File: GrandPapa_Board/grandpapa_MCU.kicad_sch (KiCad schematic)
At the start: 1 part, among them U1 DSPIC33EP512GP502

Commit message: Shameless papa copying pt 1
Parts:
- removed U1: DSPIC33EP512GP502, Package_DIP:DIP-28_W7.62mm, symbol CANHW:DSPIC33EP512GP502
- added U?: PIC18F26K83, symbol CANHW:PIC18F26K83
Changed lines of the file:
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@@
 (kicad_sch (version 20211123) (generator eeschema)
   (paper "A4")
-  (symbol (lib_id "CANHW:DSPIC33EP512GP502") (at 93.98 128.27 0) (unit 1)
+  (symbol (lib_id "CANHW:PIC18F26K83") (at 137.16 99.06 0) (unit 1)
     (in_bom yes) (on_board yes) (fields_autoplaced)
-    (property "Reference" "U1" (id 0) (at 98.5394 95.25 0)
-      (effects (font (size 1.27 1.27)) (justify left))
-    )
-    (property "Value" "DSPIC33EP512GP502" (id 1) (at 98.5394 97.79 0)
-      (effects (font (size 1.27 1.27)) (justify left))
-    )
-    (property "Footprint" "Package_DIP:DIP-28_W7.62mm" (id 2) (at 93.98 128.27 0)
+    (property "Reference" "U?" (id 0) (at 136.525 74.93 0))
+    (property "Value" "PIC18F26K83" (id 1) (at 136.525 77.47 0))
+    (property "Footprint" "" (id 2) (at 148.59 99.06 0)
       (effects (font (size 1.27 1.27)) hide)
     )
-    (property "Datasheet" "" (id 3) (at 93.98 128.27 0)
+    (property "Datasheet" "http://ww1.microchip.com/downloads/en/DeviceDoc/40001943A.pdf" (id 3) (at 148.59 99.06 0)
       (effects (font (size 1.27 1.27)) hide)
     )

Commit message: Add power circuits and some PIC stuff, grandpapa lib
5V buck, 3.3V LDO, load switches, current and voltage sensing, some PIC stuff
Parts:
- added C? (x2): 0.1uF 20V, symbol Device:C_Small
- added C? (x2): 27pF, Capacitor_SMD:C_0805_2012Metric_Pad1.18x1.45mm_HandSolder, symbol Device:C_Small
- added D?: QBLP650-IW, LED_SMD:LED_1206_3216Metric_Pad1.42x1.75mm_HandSolder, symbol Device:LED
- added D?: 150120BS75000, LED_SMD:LED_1206_3216Metric_Pad1.42x1.75mm_HandSolder, symbol Device:LED
- added D?: 156120RS75000, LED_SMD:LED_1206_3216Metric_Pad1.42x1.75mm_HandSolder, symbol Device:LED
- added J?: Programming Header, canhw_footprints:PinHeader_5x2.54_SMD_90deg_952-3198-1-ND, symbol sensors-rescue:Conn_01x05_Female-Connector
- added R? (x3): 150R, Resistor_SMD:R_0805_2012Metric_Pad1.20x1.40mm_HandSolder, symbol Device:R_Small_US
- added R?: 100R, symbol Device:R_Small_US
- added R?: 10kR, symbol Device:R_Small_US
- added Y?: 12MHz, Crystal:Crystal_HC49-4H_Vertical, symbol Device:Crystal
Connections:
- net at U?.1 (~{MCLR}): now also R?.2
- net at U?.10 (RA6/OSC2): now also C?.1, Y?.2
- net MOSI: now reaches U?.13 (RC2)
- net MOSI: now also U?.15 (RC4)
- net SCK: now reaches U?.14 (RC3)
- net at U?.16 (RC5): now also R?.1
- net at U?.17 (RC6): now also R?.1
- net at U?.18 (RC7): now also R?.1
- net GND: now reaches U?.19 (VSS)
- net GND: now also U?.8 (VSS), C?.2, C?.2, C?.2, C?.2, D?.1 (K), D?.1 (K), D?.1 (K), J?.3 (Pin_3)
- net BATT_CURR_AMP: now reaches U?.2 (RA0)
- net +3V3: now reaches U?.20 (VDD)
- net +3V3: now also C?.1, J?.2 (Pin_2), R?.1
- net MINISENSOR_PWR_EN: now reaches U?.24 (RB3)
- net STRAIN_GUAGE_AMP_PWR_EN: now reaches U?.25 (RB4)
- net LOGGER_PWR_EN: now reaches U?.26 (RB5)
- net ICSPCLK: now reaches U?.27 (RB6/ICSPCLK)
- net ICSPCLK: now also J?.5 (Pin_5)
- net ICSPDAT: now reaches U?.28 (RB7/ICSPDAT)
- net ICSPDAT: now also J?.4 (Pin_4)
- net 3V3_CURR_AMP: now reaches U?.3 (RA1)
- net V_SENSE: now reaches U?.4 (RA2)
- net CS: now reaches U?.7 (RA5)
- net at U?.9 (RA7/OSC1): now also C?.1, Y?.1
- new net: D?.2 (A), R?.2 (x3)
- new net ~{MCLR}: C?.1, J?.1 (Pin_1), R?.1, R?.2
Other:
- note added: "BLUE"
- note added: "Debugging LEDs Vs = 3.3V"
- note added: "ENABLE AT >1.3V"
- note added: "RED"
- note added: "WHITE"

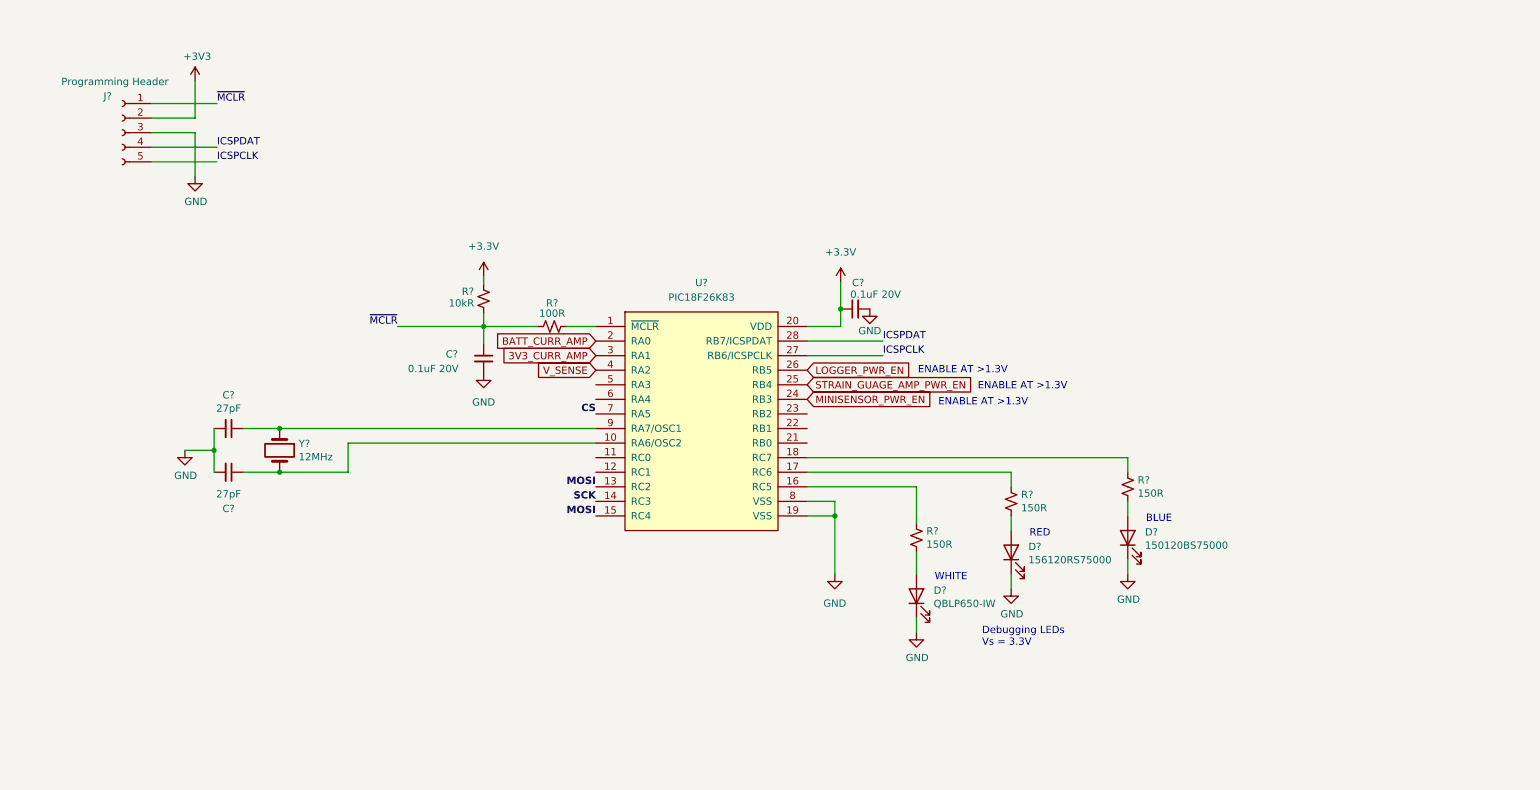
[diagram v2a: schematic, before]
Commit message: Add missing capacitor value, annotate symbols
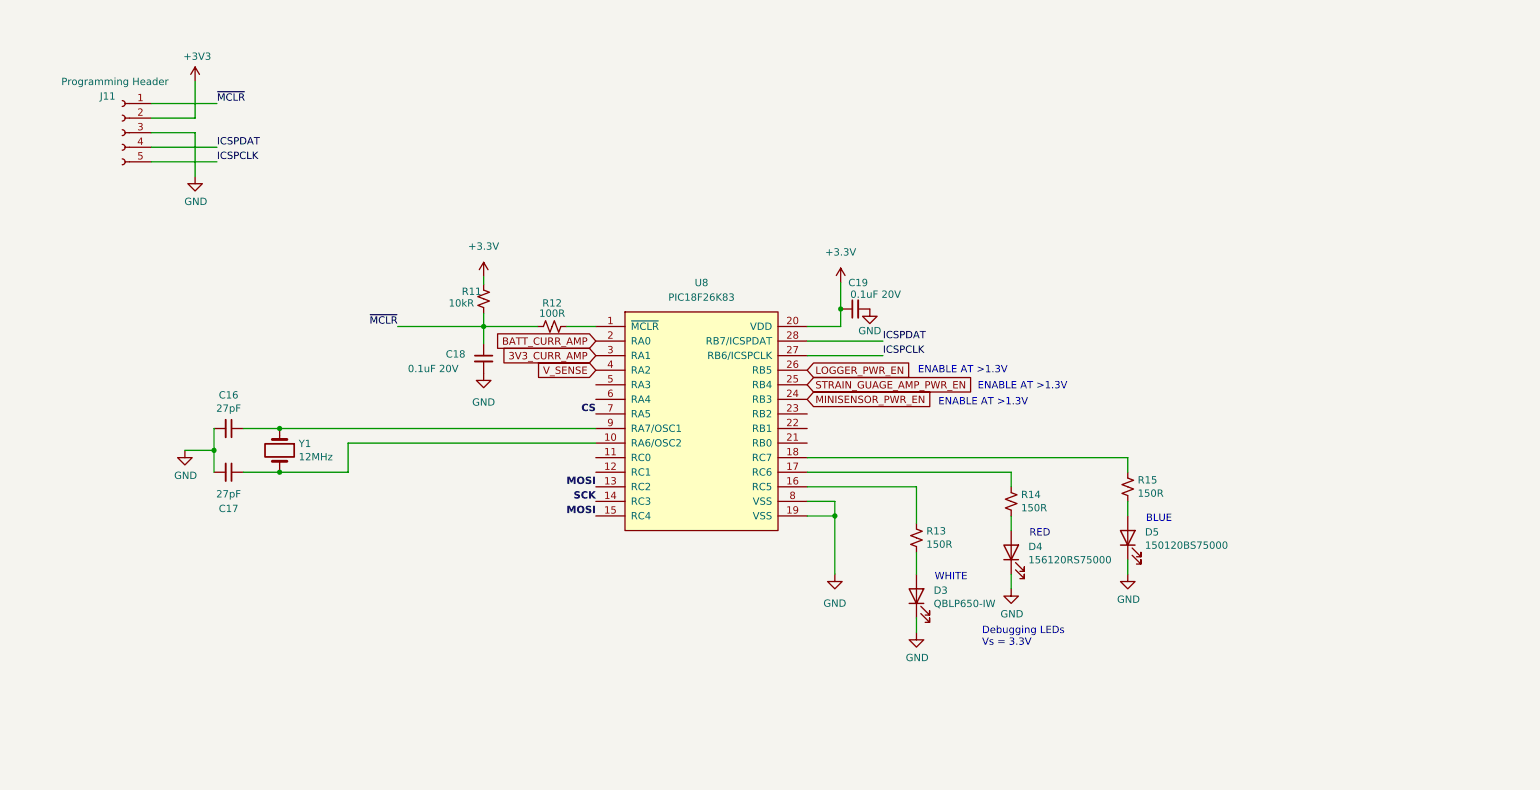
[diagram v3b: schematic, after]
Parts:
- gave numbers to parts that had none: 15
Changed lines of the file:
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@@
   (symbol (lib_id "Device:R_Small_US") (at 190.5 113.03 0) (unit 1)
     (in_bom yes) (on_board yes)
-    (property "Reference" "R?" (id 0) (at 192.2272 111.8616 0)
+    (property "Reference" "R14" (id 0) (at 192.2272 111.8616 0)
       (effects (font (size 1.27 1.27)) (justify left))
     )
@@
   (symbol (lib_id "power:+3V3") (at 48.26 39.878 0) (unit 1)
     (in_bom yes) (on_board yes)
-    (property "Reference" "#PWR?" (id 0) (at 48.26 43.688 0)
+    (property "Reference" "#PWR040" (id 0) (at 48.26 43.688 0)
       (effects (font (size 1.27 1.27)) hide)
     )
@@
   (symbol (lib_id "sensors-rescue:Conn_01x05_Female-Connector") (at 35.56 48.768 0) (mirror y) (unit 1)
     (in_bom yes) (on_board yes)
-    (property "Reference" "J?" (id 0) (at 33.02 42.418 0))
+    (property "Reference" "J11" (id 0) (at 33.02 42.418 0))
     (property "Value" "Programming Header" (id 1) (at 34.29 39.878 0))
     (property "Footprint" "canhw_footprints:PinHeader_5x2.54_SMD_90deg_952-3198-1-ND" (id 2) (at 35.56 48.768 0)
@@
   (symbol (lib_id "power:GND") (at 210.82 125.73 0) (unit 1)
     (in_bom yes) (on_board yes)
-    (property "Reference" "#PWR?" (id 0) (at 210.82 132.08 0)
+    (property "Reference" "#PWR049" (id 0) (at 210.82 132.08 0)
       (effects (font (size 1.27 1.27)) hide)
     )
@@
   (symbol (lib_id "power:GND") (at 46.482 104.14 0) (unit 1)
     (in_bom yes) (on_board yes)
-    (property "Reference" "#PWR?" (id 0) (at 46.482 110.49 0)
+    (property "Reference" "#PWR039" (id 0) (at 46.482 110.49 0)
       (effects (font (size 1.27 1.27)) hide)
     )
@@
   (symbol (lib_id "power:GND") (at 165.862 79.502 0) (unit 1)
     (in_bom yes) (on_board yes)
-    (property "Reference" "#PWR?" (id 0) (at 165.862 85.852 0)
+    (property "Reference" "#PWR046" (id 0) (at 165.862 85.852 0)
       (effects (font (size 1.27 1.27)) hide)
     )
@@
   (symbol (lib_id "Device:LED") (at 173.99 129.54 90) (unit 1)
     (in_bom yes) (on_board yes)
-    (property "Reference" "D?" (id 0) (at 176.9872 128.5494 90)
+    (property "Reference" "D3" (id 0) (at 176.9872 128.5494 90)
       (effects (font (size 1.27 1.27)) (justify right))
     )
@@
   (symbol (lib_id "power:GND") (at 159.766 125.73 0) (unit 1)
     (in_bom yes) (on_board yes) (fields_autoplaced)
-    (property "Reference" "#PWR?" (id 0) (at 159.766 132.08 0)
+    (property "Reference" "#PWR044" (id 0) (at 159.766 132.08 0)
       (effects (font (size 1.27 1.27)) hide)
     )
@@
   (symbol (lib_id "Device:C_Small") (at 98.552 88.138 0) (unit 1)
     (in_bom yes) (on_board yes)
-    (property "Reference" "C?" (id 0) (at 91.948 87.376 0)
+    (property "Reference" "C18" (id 0) (at 91.948 87.376 0)
       (effects (font (size 1.27 1.27)) (justify left))
     )
@@
   (symbol (lib_id "Device:R_Small_US") (at 173.99 119.38 0) (unit 1)
     (in_bom yes) (on_board yes)
-    (property "Reference" "R?" (id 0) (at 175.7172 118.2116 0)
+    (property "Reference" "R13" (id 0) (at 175.7172 118.2116 0)
       (effects (font (size 1.27 1.27)) (justify left))
     )
@@
   (symbol (lib_id "Device:R_Small_US") (at 210.82 110.49 0) (unit 1)
     (in_bom yes) (on_board yes)
-    (property "Reference" "R?" (id 0) (at 212.5472 109.3216 0)
+    (property "Reference" "R15" (id 0) (at 212.5472 109.3216 0)
       (effects (font (size 1.27 1.27)) (justify left))
     )
@@
   (symbol (lib_id "power:+3.3V") (at 98.552 73.914 0) (unit 1)
     (in_bom yes) (on_board yes) (fields_autoplaced)
-    (property "Reference" "#PWR?" (id 0) (at 98.552 77.724 0)
+    (property "Reference" "#PWR042" (id 0) (at 98.552 77.724 0)
       (effects (font (size 1.27 1.27)) hide)
     )
@@
   (symbol (lib_id "Device:R_Small_US") (at 110.49 82.55 90) (unit 1)
     (in_bom yes) (on_board yes)
-    (property "Reference" "R?" (id 0) (at 110.49 78.486 90))
+    (property "Reference" "R12" (id 0) (at 110.49 78.486 90))
     (property "Value" "100R" (id 1) (at 110.49 80.264 90))
     (property "Footprint" "" (id 2) (at 110.49 82.55 0)
@@
   (symbol (lib_id "power:GND") (at 98.552 90.678 0) (unit 1)
     (in_bom yes) (on_board yes) (fields_autoplaced)
-    (property "Reference" "#PWR?" (id 0) (at 98.552 97.028 0)
+    (property "Reference" "#PWR043" (id 0) (at 98.552 97.028 0)
       (effects (font (size 1.27 1.27)) hide)
     )
@@
   (symbol (lib_id "Device:C_Small") (at 163.322 79.502 90) (unit 1)
     (in_bom yes) (on_board yes)
-    (property "Reference" "C?" (id 0) (at 163.83 74.93 90))
+    (property "Reference" "C19" (id 0) (at 163.83 74.93 90))
     (property "Value" "0.1uF 20V" (id 1) (at 166.878 76.962 90))
     (property "Footprint" "" (id 2) (at 163.322 79.502 0)
@@
   (symbol (lib_id "Device:LED") (at 210.82 119.38 90) (unit 1)
     (in_bom yes) (on_board yes)
-    (property "Reference" "D?" (id 0) (at 213.8172 118.3894 90)
+    (property "Reference" "D5" (id 0) (at 213.8172 118.3894 90)
       (effects (font (size 1.27 1.27)) (justify right))
     )
@@
   (symbol (lib_id "Device:C_Small") (at 54.102 107.95 270) (unit 1)
     (in_bom yes) (on_board yes)
-    (property "Reference" "C?" (id 0) (at 54.102 114.3 90))
+    (property "Reference" "C17" (id 0) (at 54.102 114.3 90))
     (property "Value" "27pF" (id 1) (at 54.102 111.76 90))
     (property "Footprint" "Capacitor_SMD:C_0805_2012Metric_Pad1.18x1.45mm_HandSolder" (id 2) (at 54.102 107.95 0)
@@
   (symbol (lib_id "power:GND") (at 48.26 56.388 0) (unit 1)
     (in_bom yes) (on_board yes)
-    (property "Reference" "#PWR?" (id 0) (at 48.26 62.738 0)
+    (property "Reference" "#PWR041" (id 0) (at 48.26 62.738 0)
       (effects (font (size 1.27 1.27)) hide)
     )
@@
   (symbol (lib_id "power:+3.3V") (at 160.782 74.93 0) (unit 1)
     (in_bom yes) (on_board yes) (fields_autoplaced)
-    (property "Reference" "#PWR?" (id 0) (at 160.782 78.74 0)
+    (property "Reference" "#PWR045" (id 0) (at 160.782 78.74 0)
       (effects (font (size 1.27 1.27)) hide)
     )
@@
   (symbol (lib_id "Device:LED") (at 190.5 121.92 90) (unit 1)
     (in_bom yes) (on_board yes)
-    (property "Reference" "D?" (id 0) (at 193.4972 120.9294 90)
+    (property "Reference" "D4" (id 0) (at 193.4972 120.9294 90)
       (effects (font (size 1.27 1.27)) (justify right))
     )
@@
   (symbol (lib_id "CANHW:PIC18F26K83") (at 137.16 99.06 0) (unit 1)
     (in_bom yes) (on_board yes) (fields_autoplaced)
-    (property "Reference" "U?" (id 0) (at 136.525 74.93 0))
+    (property "Reference" "U8" (id 0) (at 136.525 74.93 0))
     (property "Value" "PIC18F26K83" (id 1) (at 136.525 77.47 0))
     (property "Footprint" "" (id 2) (at 148.59 99.06 0)
@@
   (symbol (lib_id "power:GND") (at 190.5 128.27 0) (unit 1)
     (in_bom yes) (on_board yes)
-    (property "Reference" "#PWR?" (id 0) (at 190.5 134.62 0)
+    (property "Reference" "#PWR048" (id 0) (at 190.5 134.62 0)
       (effects (font (size 1.27 1.27)) hide)
     )
@@
   (symbol (lib_id "Device:C_Small") (at 54.102 100.33 270) (unit 1)
     (in_bom yes) (on_board yes)
-    (property "Reference" "C?" (id 0) (at 54.102 94.5134 90))
+    (property "Reference" "C16" (id 0) (at 54.102 94.5134 90))
     (property "Value" "27pF" (id 1) (at 54.102 96.8248 90))
     (property "Footprint" "Capacitor_SMD:C_0805_2012Metric_Pad1.18x1.45mm_HandSolder" (id 2) (at 54.102 100.33 0)
@@
   (symbol (lib_id "Device:R_Small_US") (at 98.552 77.724 0) (unit 1)
     (in_bom yes) (on_board yes)
-    (property "Reference" "R?" (id 0) (at 94.742 76.454 0)
+    (property "Reference" "R11" (id 0) (at 94.742 76.454 0)
       (effects (font (size 1.27 1.27)) (justify left))
     )
@@
   (symbol (lib_id "Device:Crystal") (at 62.992 104.14 270) (unit 1)
     (in_bom yes) (on_board yes)
-    (property "Reference" "Y?" (id 0) (at 66.3194 102.9716 90)
+    (property "Reference" "Y1" (id 0) (at 66.3194 102.9716 90)
       (effects (font (size 1.27 1.27)) (justify left))
     )
@@
   (symbol (lib_id "power:GND") (at 173.99 135.89 0) (unit 1)
     (in_bom yes) (on_board yes)
-    (property "Reference" "#PWR?" (id 0) (at 173.99 142.24 0)
-      (effects (font (size 1.27 1.27)) hide)
-    )
+    (property "Reference" "#PWR047" (id 0) (at 173.99 142.24 0)
+      (effects (font (size 1.27 1.27)) hide)
+    )

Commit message: Add motor current sense amp and board output connections
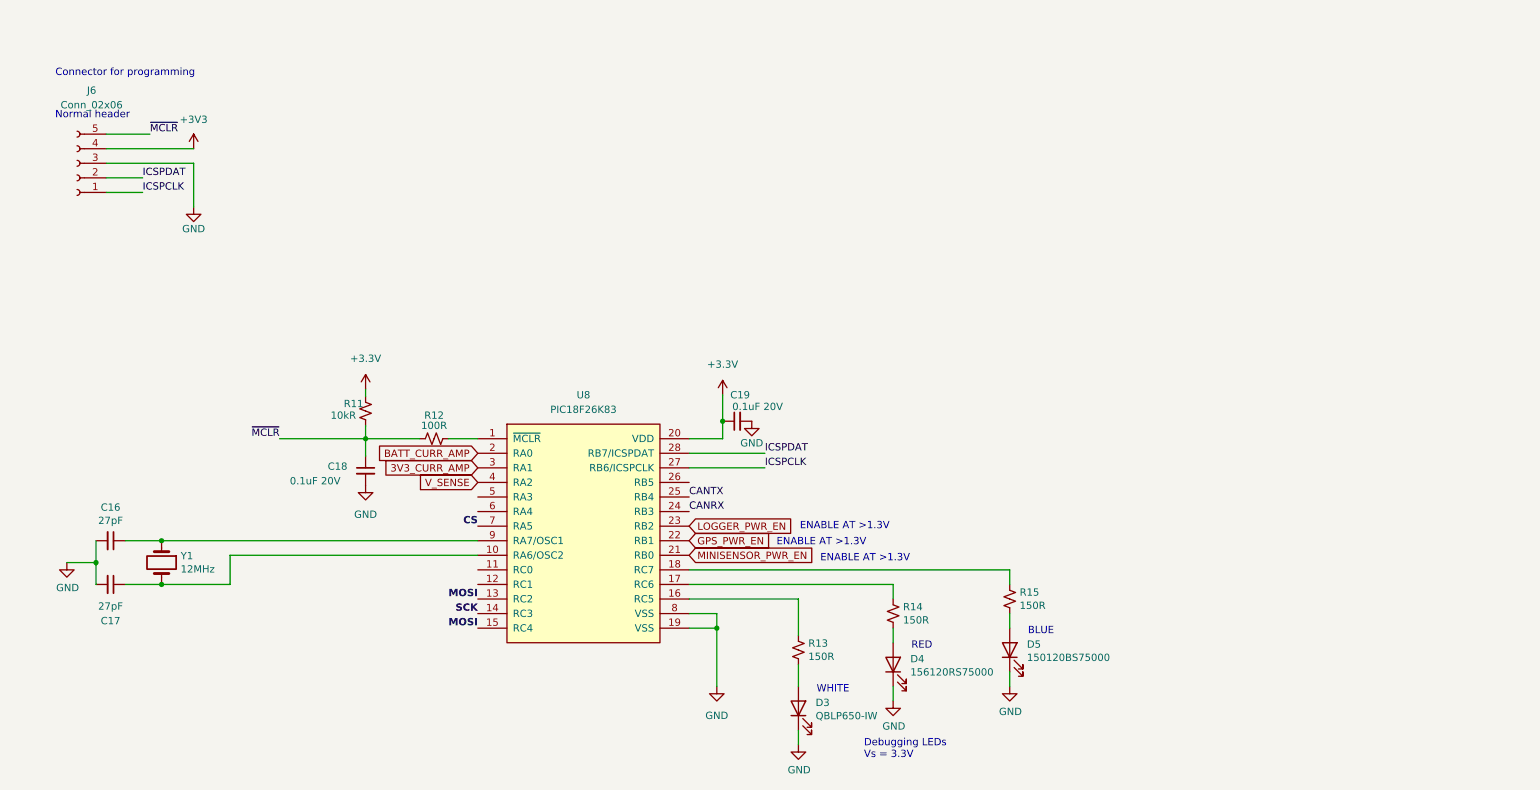
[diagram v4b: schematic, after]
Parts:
- removed J11: Programming Header, canhw_footprints:PinHeader_5x2.54_SMD_90deg_952-3198-1-ND, symbol sensors-rescue:Conn_01x05_Female-Connector
- added J6: Conn_02x06, Connector_PinHeader_2.54mm:PinHeader_1x05_P2.54mm_Vertical, symbol Connector:Conn_01x05_Female
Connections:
- net +3V3: now also J6.4 (Pin_4)
- net GND: now also J6.3 (Pin_3)
- net ICSPCLK: now also J6.1 (Pin_1)
- net ICSPDAT: now also J6.2 (Pin_2)
- net LOGGER_PWR_EN: now also U8.23 (RB2); no longer U8.26 (RB5)
- net MINISENSOR_PWR_EN: now also U8.21 (RB0); no longer U8.24 (RB3)
- net ~{MCLR}: now also J6.5 (Pin_5)
- net GPS_PWR_EN: now reaches U8.22 (RB1)
- net STRAIN_GUAGE_AMP_PWR_EN renamed CANTX
- new net CANRX: U8.24 (RB3)
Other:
- note added: "Connector for programming"
- note added: "Normal header"
- moved on the sheet: C16, C17, C18, C19, D3, D4, D5, R11, R12, R13, R14, R15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
